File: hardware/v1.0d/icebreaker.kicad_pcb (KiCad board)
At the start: 4 copper layers, 73 x 37 mm, 191 parts, among them J1 Jumper, J10 Jumper, J11 Jumper, J12 Jumper, J13 Jumper, J14 Jumper, J15 Jumper, J16 Jumper, J17 Jumper, J18 Jumper, J19 Jumper, J2 Jumper, J20 Flash, J21 PMOD, J22 PMOD, J23 PMOD, J24 PMOD, J25 RGB Led, J26 5V AUX, J27 5V AUX, J28 CRESET, J29 Jumper, J3 Jumper, J30 Jumper, J31 RGB Led, J32 WS2812, J33 RGB Led, J34 SADD, J4 Jumper, J5 Jumper, J6 Jumper, J7 Jumper, J8 Jumper, J9 Jumper, P1 pkl_USB_OTG, P2 UP, P3 UP, P4 UP, P5 UP, P6 RAM_CS, Q1 BSS138, SW1 TACT, SW2 TACT, SW3 TACT, SW4 TACT, U1 93C46B-SOT-23-6, U2 3.3V, U3 1V2, U4 FT2232H, U5 W25Q, U6 ICE5LP4K-SG48, U7 12MHz

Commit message: Fixed RGB LED labling. Replaced RGB LED signals to be color agnostic.
The FPGA does not care which color is connected to which pin, so
referring to the pins as red, green and blue is bit silly. The signals
are now RGB0-2 instead. The only place where we label the colors are on
the actual Cree LED package pins.

This fixes #22
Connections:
- net /~LED_BLU renamed /~LED_RGB0
- net /~LED_GRN renamed /~LED_RGB1
- net /~LED_RED renamed /~LED_RGB2
- J31 pad 1: /ET_OD2 -> (no net)
- J31 pad 3: /ET_1V2 -> (no net)
- J31 pad 4: /ET_OD3 -> (no net)
- J33 pad 3: /EB_1V2 -> (no net)
- J33 pad 4: /EB_OD3 -> (no net)
- J33 pad 7: /EB_5V -> (no net)
- P1 pad 4: Net-(P1-Pad4) -> (no net)
- U4 pad 22: Net-(U4-Pad22) -> (no net)
- U4 pad 26: Net-(U4-Pad26) -> (no net)
- U4 pad 27: Net-(U4-Pad27) -> (no net)
- U4 pad 28: Net-(U4-Pad28) -> (no net)
- U4 pad 29: Net-(U4-Pad29) -> (no net)
- U4 pad 3: Net-(U4-Pad3) -> (no net)
- U4 pad 30: Net-(U4-Pad30) -> (no net)
- U4 pad 32: Net-(U4-Pad32) -> (no net)
- U4 pad 33: Net-(U4-Pad33) -> (no net)
- U4 pad 34: Net-(U4-Pad34) -> (no net)
- U4 pad 36: Net-(U4-Pad36) -> (no net)
- U4 pad 57: Net-(U4-Pad57) -> (no net)
- U4 pad 58: Net-(U4-Pad58) -> (no net)
- U4 pad 59: Net-(U4-Pad59) -> (no net)
- U4 pad 60: Net-(U4-Pad60) -> (no net)
- U7 pad 2: Net-(U7-Pad2) -> (no net)
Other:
- board text added: "(C) 2019 1Bitsquared"
- board text added: "0"
- board text added: "1B2 (C) 2019 CC-BY-SA 4.0"
- board text added: "2"
- board text added: "RGB0 1V2"
- board text added: "RGB2 RGB1"
- board text removed: "(C) 2018 1Bitsquared"
- board text removed: "1B2 (C) 2018 CC-BY-SA 4.0"
- board text removed: "BLU 1V2"
- board text removed: "RED GRN"

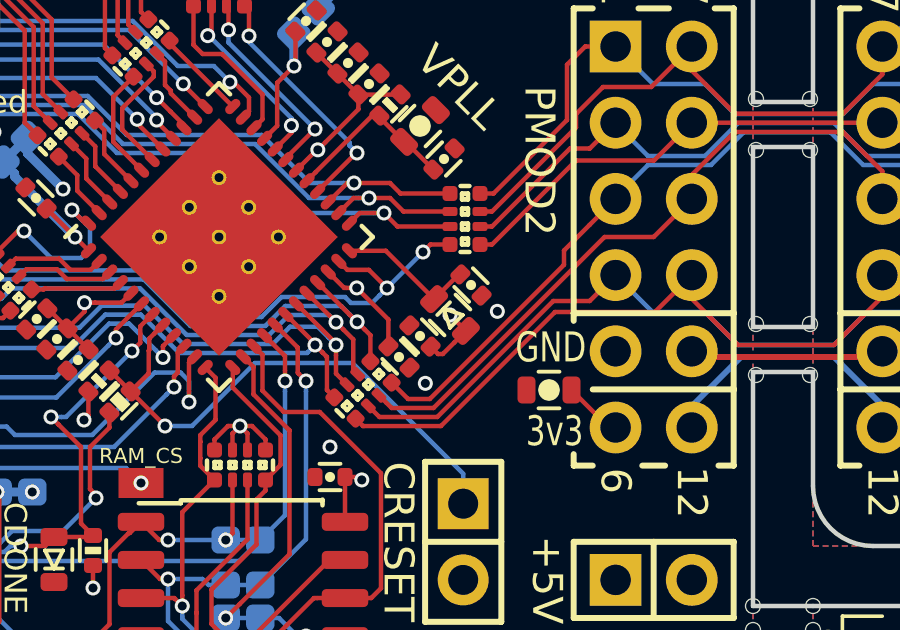
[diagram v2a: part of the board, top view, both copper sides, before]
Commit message: Changed the VPP_2V5 diode footprint to SOD-523.
The SOD-523 is more common. While I was at it I also named the VPP_2V5
net.

This fixes #26
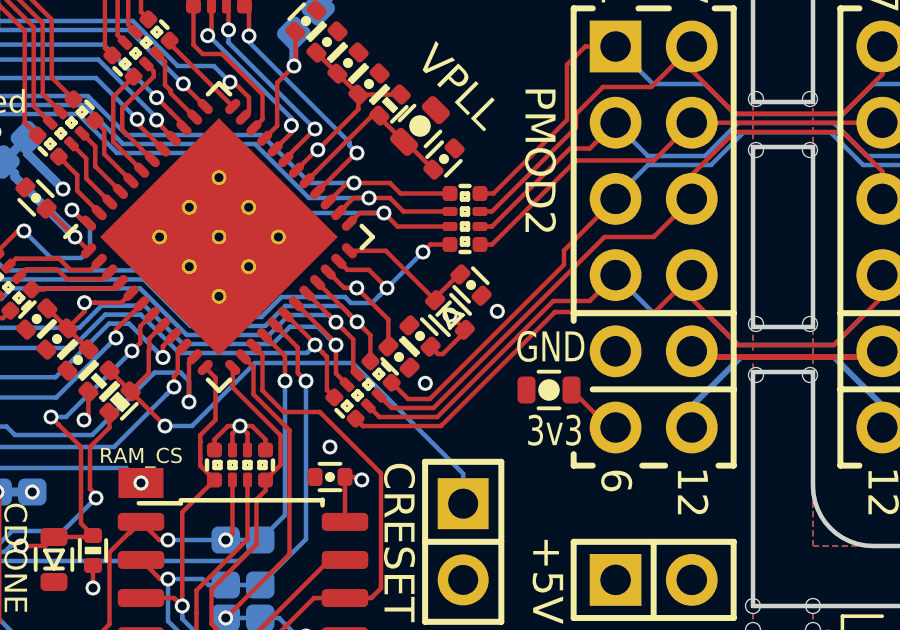
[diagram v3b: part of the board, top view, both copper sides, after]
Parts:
- D2: value CDBU0520 -> ~~800mVf; footprint pkl_dipol:D_0603 -> pkl_dipol:D_SOD-523
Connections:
- net Net-(C35-Pad1) renamed /VPP_2V5
